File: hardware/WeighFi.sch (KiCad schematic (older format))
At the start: 24 parts, among them J1 USB, P1 CONN_1, P2 CONN_1, P3 CONN_1, U1 MAX1555, U2 MCP1700

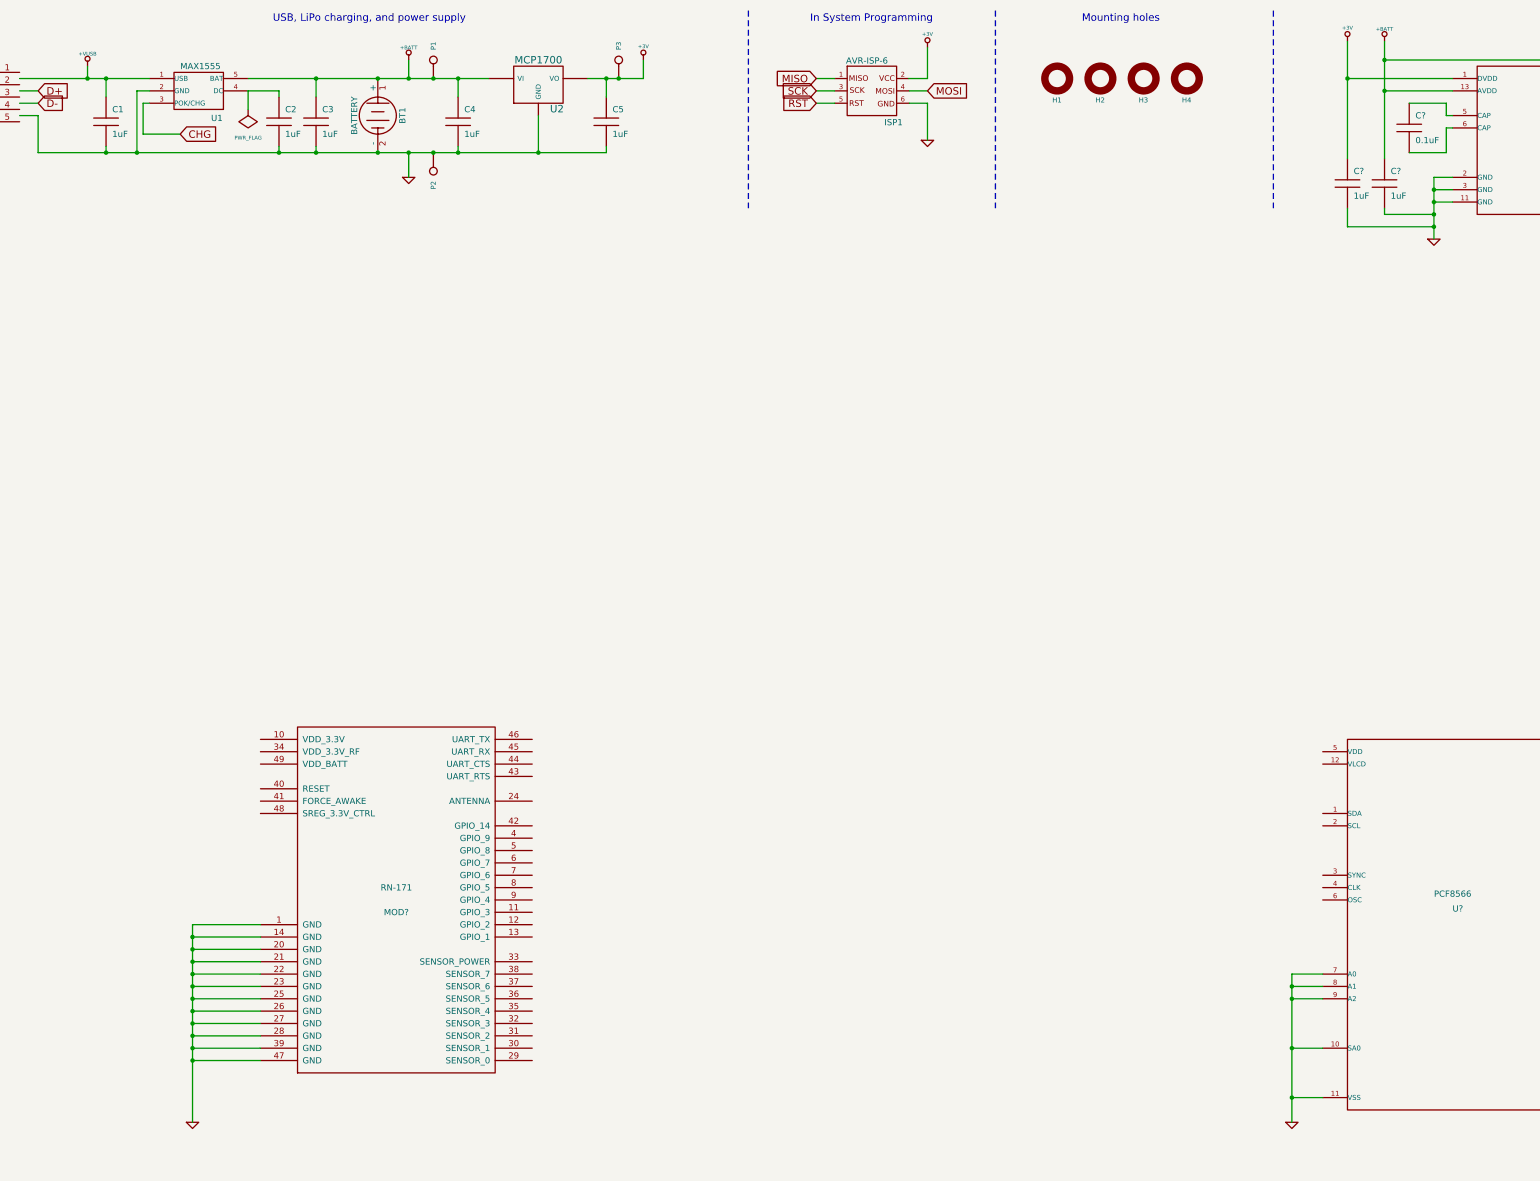
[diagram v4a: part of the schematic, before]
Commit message: RN-171 - use GPIO 4 for association status
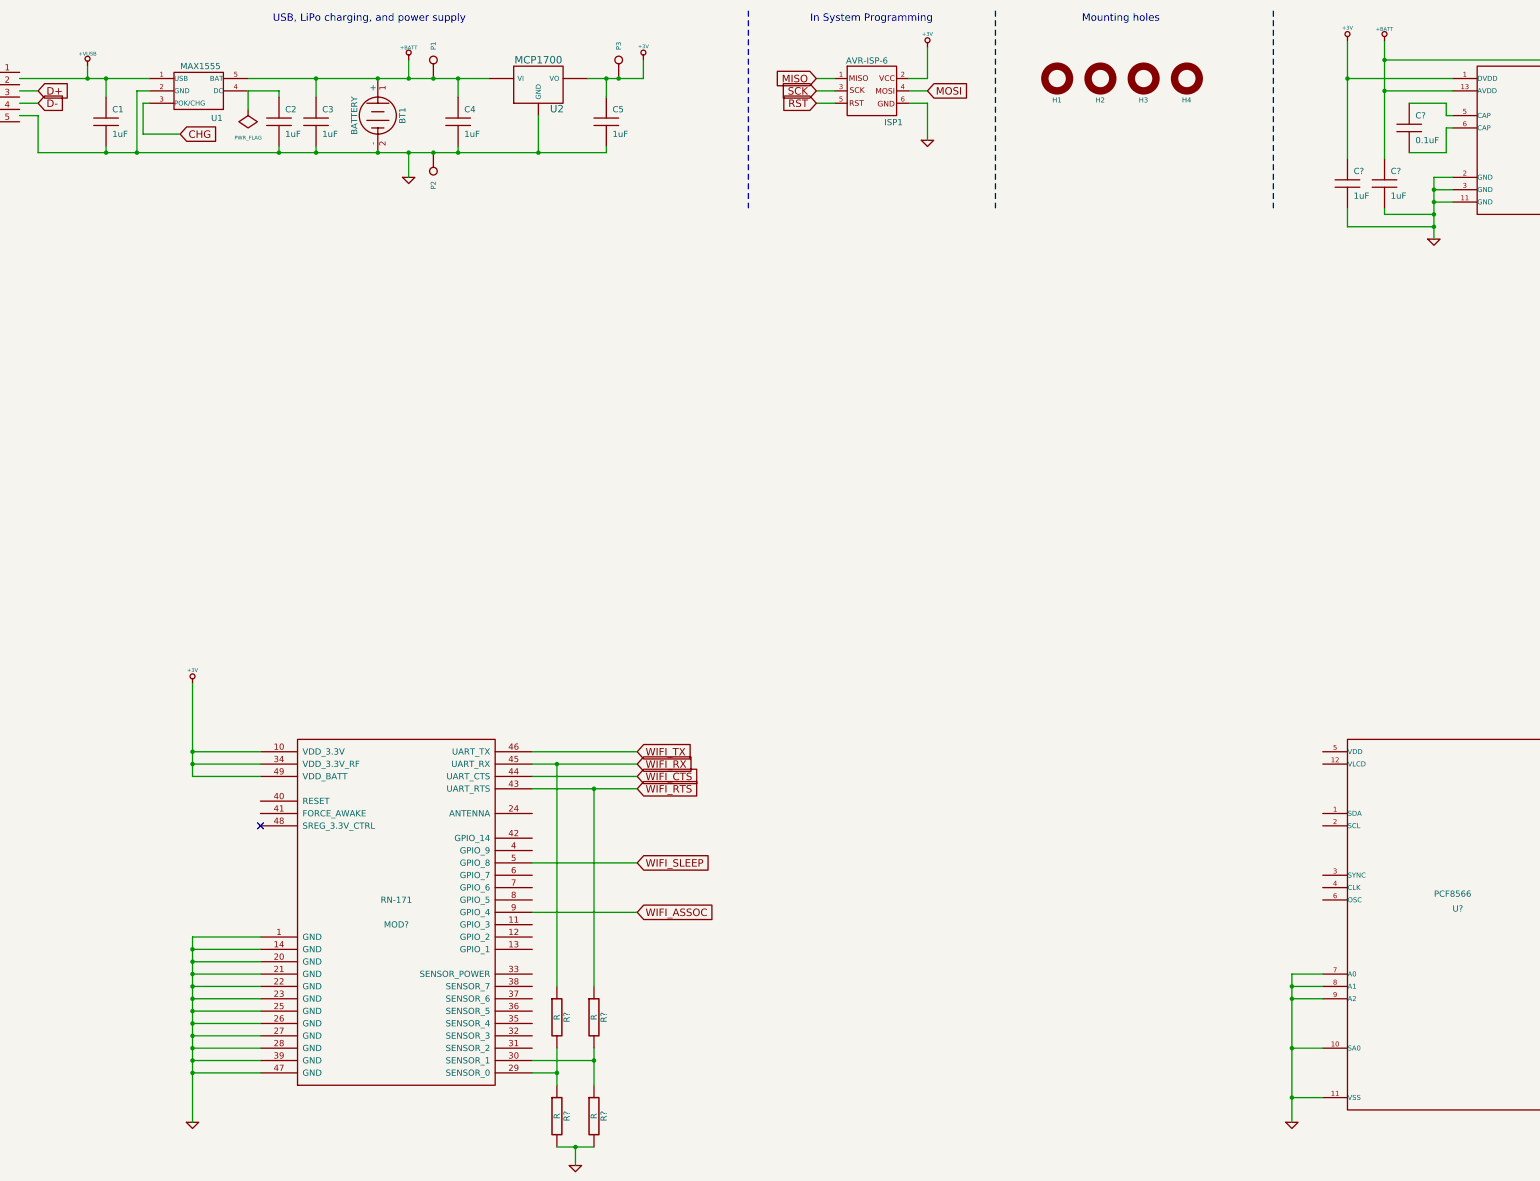
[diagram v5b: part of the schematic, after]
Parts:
- added R? (x4): R, symbol R
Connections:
- net labels added: WIFI_ASSOC, WIFI_CTS, WIFI_RTS, WIFI_RX, WIFI_SLEEP, WIFI_TX
- wire segments 156 -> 181
- no-connect marks 15 -> 16
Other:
- moved on the sheet: MOD?
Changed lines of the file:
@@
-EESchema Schematic File Version 2  date Mon 14 May 2012 09:05:37 BST
+EESchema Schematic File Version 2  date Thu 17 May 2012 14:21:02 BST
 LIBS:dresco
 LIBS:power
@@
 Sheet 1 1
 Title "WeighFi"
-Date "14 may 2012"
+Date "17 may 2012"
 Rev "1.0"
 Comp ""
@@
 Comment4 ""
 $EndDescr
-Connection ~ 2600 9100
-Wire Wire Line
-	3150 9100 2600 9100
-Connection ~ 2600 8900
-Wire Wire Line
-	3150 8900 2600 8900
-Connection ~ 2600 8700
-Wire Wire Line
-	3150 8700 2600 8700
-Connection ~ 2600 8500
-Wire Wire Line
-	3150 8500 2600 8500
-Connection ~ 2600 8300
-Wire Wire Line
-	3150 8300 2600 8300
-Connection ~ 2600 8100
-Wire Wire Line
-	3150 8100 2600 8100
+Wire Wire Line
+	6200 7900 5350 7900
+Wire Wire Line
+	5350 7500 6200 7500
+Connection ~ 5550 6700
+Wire Wire Line
+	5550 8500 5550 6700
+Wire Wire Line
+	5850 9300 5850 9100
+Wire Wire Line
+	5850 9100 5850 9000
+Wire Wire Line
+	5700 9950 5700 9800
+Connection ~ 2600 6700
+Wire Wire Line
+	3150 6700 2600 6700
+Wire Wire Line
+	5350 6900 5850 6900
+Wire Wire Line
+	5850 6900 6200 6900
+Wire Wire Line
+	5350 6700 5550 6700
+Wire Wire Line
+	5550 6700 6200 6700
+Connection ~ 2600 9200
+Wire Wire Line
+	2600 9200 3150 9200
+Connection ~ 2600 9000
+Wire Wire Line
+	2600 9000 3150 9000
+Connection ~ 2600 8800
+Wire Wire Line
+	2600 8800 3150 8800
+Connection ~ 2600 8600
+Wire Wire Line
+	2600 8600 3150 8600
+Connection ~ 2600 8400
+Wire Wire Line
+	2600 8400 3150 8400
+Connection ~ 2600 8200
+Wire Wire Line
+	3150 8200 2600 8200
 Wire Notes Line
 	11350 600  11350 2200
@@
 	12250 1000 12250 850
 Wire Wire Line
-	12800 1250 12250 1250
+	12250 1250 12800 1250
 Connection ~ 12650 2050
 Wire Wire Line
@@
 	1200 1350 1350 1350
 Wire Wire Line
-	1750 1150 1750 1050
+	1750 1050 1750 1150
 Wire Wire Line
 	2150 1750 2150 1250
@@
 Connection ~ 3600 1150
 Wire Wire Line
-	3600 1300 3600 1150
-Wire Wire Line
-	1900 1300 1900 1150
+	3600 1150 3600 1300
+Wire Wire Line
+	1900 1150 1900 1300
 Connection ~ 4550 1750
 Connection ~ 4550 1150
@@
 	8550 1150 8550 900
 Wire Wire Line
-	4750 1150 4750 1300
+	4750 1300 4750 1150
 Connection ~ 2150 1750
 Wire Wire Line
@@
 	12750 1750 12450 1750
 Wire Wire Line
-	3150 8000 2600 8000
-Wire Wire Line
-	2600 8000 2600 8100
+	3150 8100 2600 8100
 Wire Wire Line
 	2600 8100 2600 8200
@@
 	2600 9000 2600 9100
 Wire Wire Line
-	2600 9100 2600 9600
-Wire Wire Line
-	3150 8200 2600 8200
-Connection ~ 2600 8200
-Wire Wire Line
-	3150 8400 2600 8400
-Connection ~ 2600 8400
-Wire Wire Line
-	3150 8600 2600 8600
-Connection ~ 2600 8600
-Wire Wire Line
-	3150 8800 2600 8800
-Connection ~ 2600 8800
-Wire Wire Line
-	3150 9000 2600 9000
-Connection ~ 2600 9000
+	2600 9100 2600 9200
+Wire Wire Line
+	2600 9200 2600 9600
+Wire Wire Line
+	2600 8300 3150 8300
+Connection ~ 2600 8300
+Wire Wire Line
+	2600 8500 3150 8500
+Connection ~ 2600 8500
+Wire Wire Line
+	2600 8700 3150 8700
+Connection ~ 2600 8700
+Wire Wire Line
+	2600 8900 3150 8900
+Connection ~ 2600 8900
+Wire Wire Line
+	2600 9100 3150 9100
+Connection ~ 2600 9100
+Wire Wire Line
+	5350 6600 6200 6600
+Wire Wire Line
+	5350 6800 6200 6800
+Wire Wire Line
+	3150 6800 2600 6800
+Wire Wire Line
+	2600 6800 2600 6700
+Wire Wire Line
+	2600 6700 2600 6600
+Wire Wire Line
+	2600 6600 2600 6050
+Wire Wire Line
+	3150 6600 2600 6600
+Connection ~ 2600 6600
+Wire Wire Line
+	5550 9800 5700 9800
+Wire Wire Line
+	5700 9800 5850 9800
+Connection ~ 5700 9800
+Wire Wire Line
+	5550 9300 5550 9200
+Wire Wire Line
+	5550 9200 5550 9000
+Wire Wire Line
+	5850 8500 5850 6900
+Connection ~ 5850 6900
+Wire Wire Line
+	5350 9100 5850 9100
+Connection ~ 5850 9100
+Wire Wire Line
+	5350 9200 5550 9200
+Connection ~ 5550 9200
+Text GLabel 6200 7900 2    60   Input ~ 0
+WIFI_ASSOC
+Text GLabel 6200 7500 2    60   Input ~ 0
+WIFI_SLEEP
+$Comp
+L GND #PWR?
+U 1 1 4FB1371E
+P 5700 9950
+F 0 "#PWR?" H 5700 9950 30  0001 C CNN
+F 1 "GND" H 5700 9880 30  0001 C CNN
+	1    5700 9950
+	1    0    0    -1
+$EndComp
+$Comp
+L R R?
+U 1 1 4FB136EA
+P 5550 8750
+F 0 "R?" V 5630 8750 50  0000 C CNN
+F 1 "R" V 5550 8750 50  0000 C CNN
+	1    5550 8750
+	1    0    0    -1
+$EndComp
+$Comp
+L R R?
+U 1 1 4FB136E9
+P 5550 9550
+F 0 "R?" V 5630 9550 50  0000 C CNN
+F 1 "R" V 5550 9550 50  0000 C CNN
+	1    5550 9550
+	1    0    0    -1
+$EndComp
+$Comp
+L R R?
+U 1 1 4FB136DD
+P 5850 9550
+F 0 "R?" V 5930 9550 50  0000 C CNN
+F 1 "R" V 5850 9550 50  0000 C CNN
+	1    5850 9550
+	1    0    0    -1
+$EndComp
+$Comp
+L R R?
+U 1 1 4FB136DA
+P 5850 8750
+F 0 "R?" V 5930 8750 50  0000 C CNN
+F 1 "R" V 5850 8750 50  0000 C CNN
+	1    5850 8750
+	1    0    0    -1
+$EndComp
+$Comp
+L +3V #PWR?
+U 1 1 4FB1357C
+P 2600 6050
+F 0 "#PWR?" H 2600 5960 30  0001 C CNN
+F 1 "+3V" H 2600 6160 30  0000 C CNN
+	1    2600 6050
+	1    0    0    -1
+$EndComp
+NoConn ~ 3150 7200
+Text GLabel 6200 6900 2    60   Input ~ 0
+WIFI_RTS
+Text GLabel 6200 6800 2    60   Input ~ 0
+WIFI_CTS
+Text GLabel 6200 6700 2    60   Input ~ 0
+WIFI_RX
+Text GLabel 6200 6600 2    60   Input ~ 0
+WIFI_TX
 $Comp
 L GND #PWR?
@@
 L RN-171 MOD?
 U 1 1 4FB0BBD2
-P 4250 7800
-F 0 "MOD?" H 4250 7700 50  0000 C CNN
-F 1 "RN-171" H 4250 7900 50  0000 C CNN
-	1    4250 7800
-	1    0    0    -1
-$EndComp
+P 4250 7900
+F 0 "MOD?" H 4250 7800 50  0000 C CNN
+F 1 "RN-171" H 4250 8000 50  0000 C CNN
+	1    4250 7900
+	1    0    0    -1
+$EndComp

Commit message: Add ATMEGA32U4 to schematic
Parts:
- added C? (x5): 0.1uF, symbol C
- added L?: INDUCTOR, symbol INDUCTOR
- added R?: R, symbol R
- added U?: ATMEGA16U4/32U4, symbol ATMEGA16U4/32U4
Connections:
- net +3V: now also C?.1, C?.1, L?.1, R?.2, U?.14 (VCC), U?.34 (VCC)
- net GND: now also C?.2, C?.2, C?.2, C?.2, C?.2, U?.15 (GND), U?.23 (GND), U?.35 (GND), U?.42 (AREF), U?.43 (GND)
- new net: R?.1, U?.13 (RESET)
- new net: C?.1, C?.1, L?.2, U?.24 (AVCC), U?.44 (AVCC)
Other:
- moved on the sheet: MOD?, P?, R?, U?

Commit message: Add USB and other supporting circuitry for ATMEGAU324
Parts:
- removed U?: ATMEGA16U4/32U4, symbol ATMEGA16U4/32U4
- added C? (x2): 22pF, symbol C
- added C?: 1uF, symbol C
- added C?: 10uF, symbol C
- added R? (x2): 22, symbol R
- added U?: ATMEGA16U4/32U4, symbol ATMEGA16U4/32U4
- added USB?: USB, symbol USB
- added X?: CRYSTAL, symbol CRYSTAL
- R?: value R -> 10K
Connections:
- net +3V: now also C?.1, U?.14 (VCC), U?.34 (VCC), U?.6 (UCap)
- net GND: now also C?.1, C?.1, C?.1, C?.2, U?.15 (GND), U?.23 (GND), U?.35 (GND), U?.43 (GND), U?.5 (UGnd), USB?.5 (GND)
- net at R?.1: now also U?.13 (RESET)
- net at C?.1, C?.1, L?.2: now also U?.24 (AVCC), U?.44 (AVCC)
- net at C?.1: now also U?.42 (AREF)
- new net: C?.2, U?.16 (XTAL2), X?.1
- new net: C?.2, U?.17 (XTAL1), X?.2
- new net: R?.2, U?.3 (D-)
- new net: R?.2, U?.4 (D+)
- new net: C?.2, U?.7 (VBus), USB?.1 (VBUS)
- new net: R?.1, USB?.2 (D+)
- new net: R?.1, USB?.3 (D-)
- no-connect marks 16 -> 18
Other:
- moved on the sheet: C?

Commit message: More supporting circuitry
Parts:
- removed J1: USB, symbol USB
- added ANT?: ANTENNA, symbol ANTENNA
- added Q?: MOSFET_P, symbol MOSFET_P
- added R? (x2): 4K7, symbol R
- added R?: 100K, symbol R
- added R?: 100, symbol R
- added SJ? (x2): SOLDER_JUMPER, symbol SOLDER_JUMPER
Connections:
- net SCK is gone; now on net SCLK: ISP1.3
- net +3V: now also Q?.S, R?.2
- net +VUSB: now also C?.2, U?.7 (VBus), USB?.1 (VBUS)
- net D+: now also R?.1, USB?.2 (D+)
- net D-: now also R?.1, USB?.3 (D-)
- net GND: now also U?.12 (VLCD), SJ?.1
- net MISO: now also U?.11 ((PCINT3/PDO/MISO)_PB3)
- net MOSI: now also U?.10 ((PCINT2/PDI/MOSI)_PB2)
- net RST: now also R?.1, U?.13 (RESET)
- net I2C_DATA: now reaches U?.1 (SDA)
- net I2C_DATA: now also U?.19 ((SDA/INT1)_PD1), R?.2
- net I2C_CLOCK: now reaches U?.2 (SCL)
- net I2C_CLOCK: now also U?.20 ((RXD1/INT2)_PD2), R?.2
- net LCD_CLOCK: now reaches U?.4 (CLK)
- net LCD_SUPPLY: now reaches U?.5 (VDD)
- net LCD_SUPPLY: now also Q?.D, R?.1, R?.1, SJ?.1
- net at U?.6 (OSC): now also SJ?.2, SJ?.2
- net ADC_PWRDN: now reaches U?.14 (PDWN)
- net ADC_CLOCK: now reaches U?.15 (SCLK)
- net ADC_DATA: now reaches U?.16 (DRDY/DOUT)
- net ADC_SPEED: now reaches U?.4 (SPEED)
- net at MOD?.24 (ANTENNA): now also ANT?.~
- net SCLK: now reaches U?.9 ((PCINT1/SCLK)_PB1)
- new net: Q?.G, R?.1, R?.2
- new net LCD_ENABLE: R?.1
- no-connect marks 18 -> 19
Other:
- moved on the sheet: C?, P?, R?, U?, USB?
